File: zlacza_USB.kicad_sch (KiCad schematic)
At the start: 16 parts, among them J1 USB_C_Receptacle_USB2.0_16P, J11 Conn 5 USB 1 A, J12 Conn 5 USB 1 B, J13 Conn_19 USBC FULL 1B, J14 USB_C_Receptacle FULL 2, J15 USB3_A_Stacked, J16 Conn 10 USB3 A1 A, J17 USB_C_Receptacle FULL 1, J20 Conn_ 19USBC FULL 1A, J21 Conn 19 USBC FULL 2A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

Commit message: Update  conector usb.
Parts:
- J1: footprint (none) -> Connector_USB:USB_C_Receptacle_G-Switch_GT-USB-7010ASV
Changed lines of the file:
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@@
 			)
 		)
-		(property "Footprint" ""
+		(property "Footprint" "Connector_USB:USB_C_Receptacle_G-Switch_GT-USB-7010ASV"
 			(at -10.16 148.59 0)
 			(effects

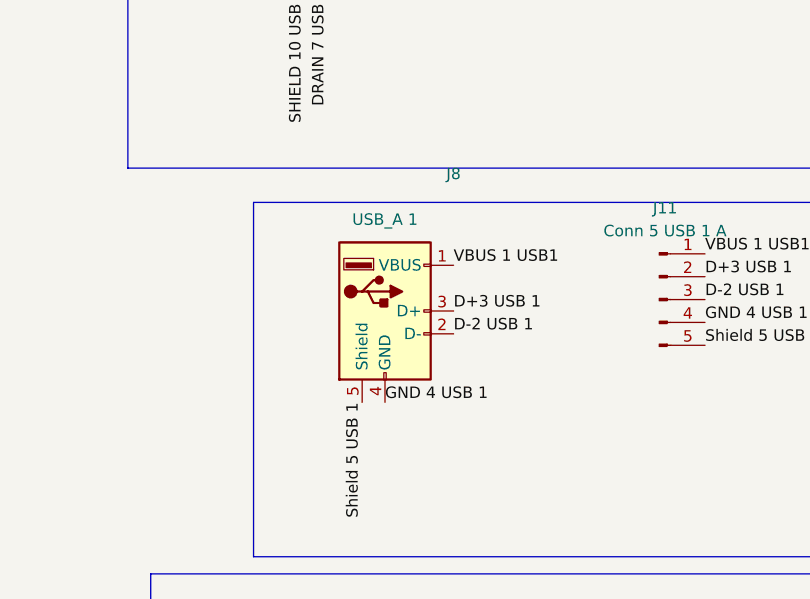
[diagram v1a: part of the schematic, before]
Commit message: symbole i footprinty #1
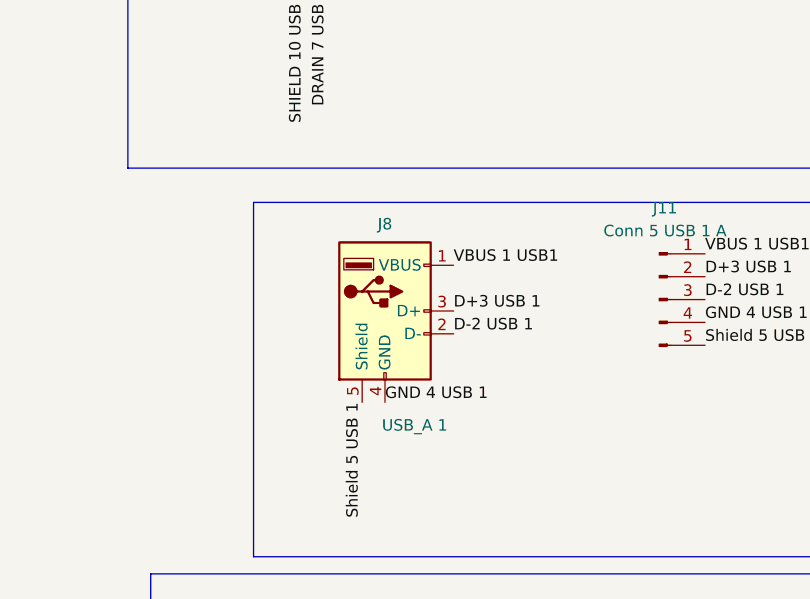
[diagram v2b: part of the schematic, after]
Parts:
- J8: footprint Connector_USB:USB_A_CONNFLY_DS1095-WNR0 -> Connector_USB:USB_A_Connfly_DS1095
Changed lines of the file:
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@@
 		(dnp no)
 		(property "Reference" "J8"
-			(at 50.8 76.2 0)
+			(at 43.18 81.788 0)
 			(effects
 				(font
@@
 		)
 		(property "Value" "USB_A 1"
-			(at 43.18 81.28 0)
+			(at 46.482 104.14 0)
 			(effects
 				(font
@@
 			)
 		)
-		(property "Footprint" "Connector_USB:USB_A_CONNFLY_DS1095-WNR0"
+		(property "Footprint" "Connector_USB:USB_A_Connfly_DS1095"
 			(at 46.99 92.71 0)
 			(effects
